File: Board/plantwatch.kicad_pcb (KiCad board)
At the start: 2 copper layers, 113 x 83.8 mm, 39 parts, among them IC1 HS1101, J1 Motor, J2 SEN0193, J3 SWD, J6 Power Input, Q1 BSP129, SW1 Reset, U1 MKL25Z128VLK4, U2 TMP36, U3 nRF24L01+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

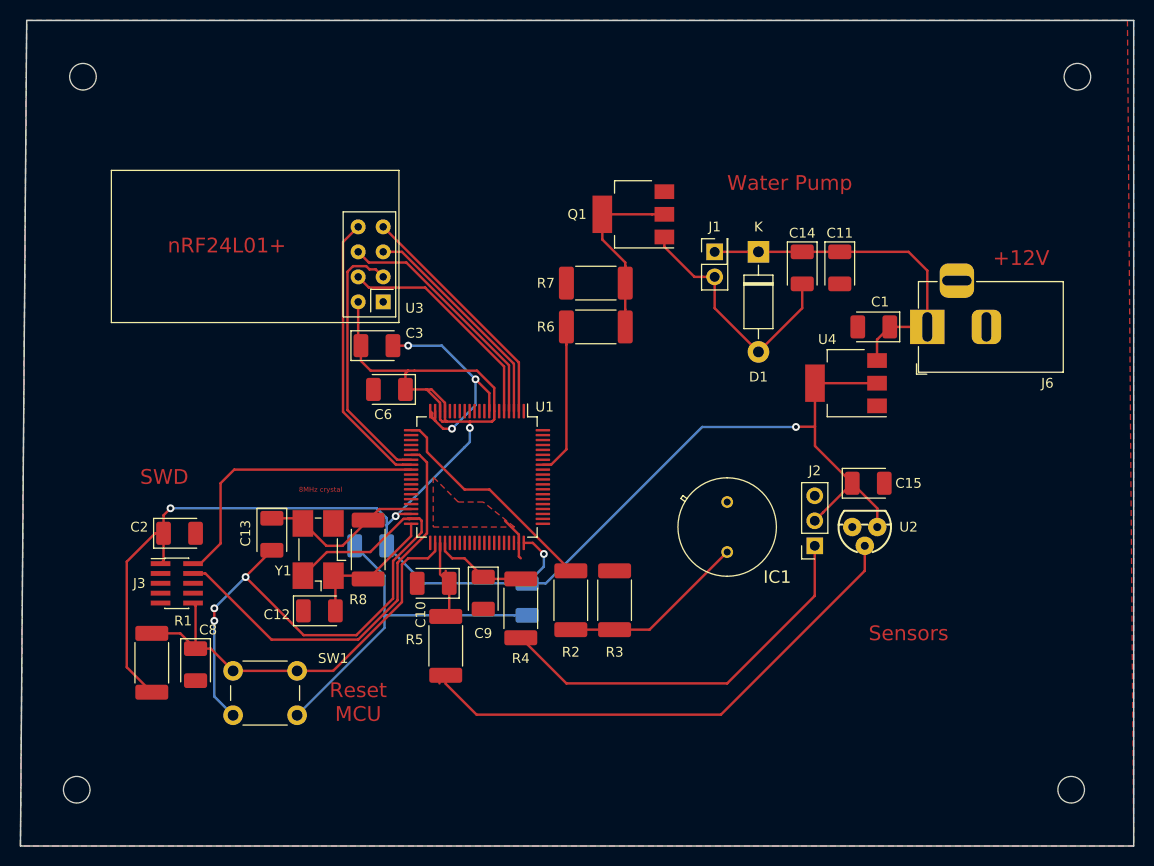
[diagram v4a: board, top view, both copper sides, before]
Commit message: SWD connector footprint pitch 1.0mm -> 1.27mm
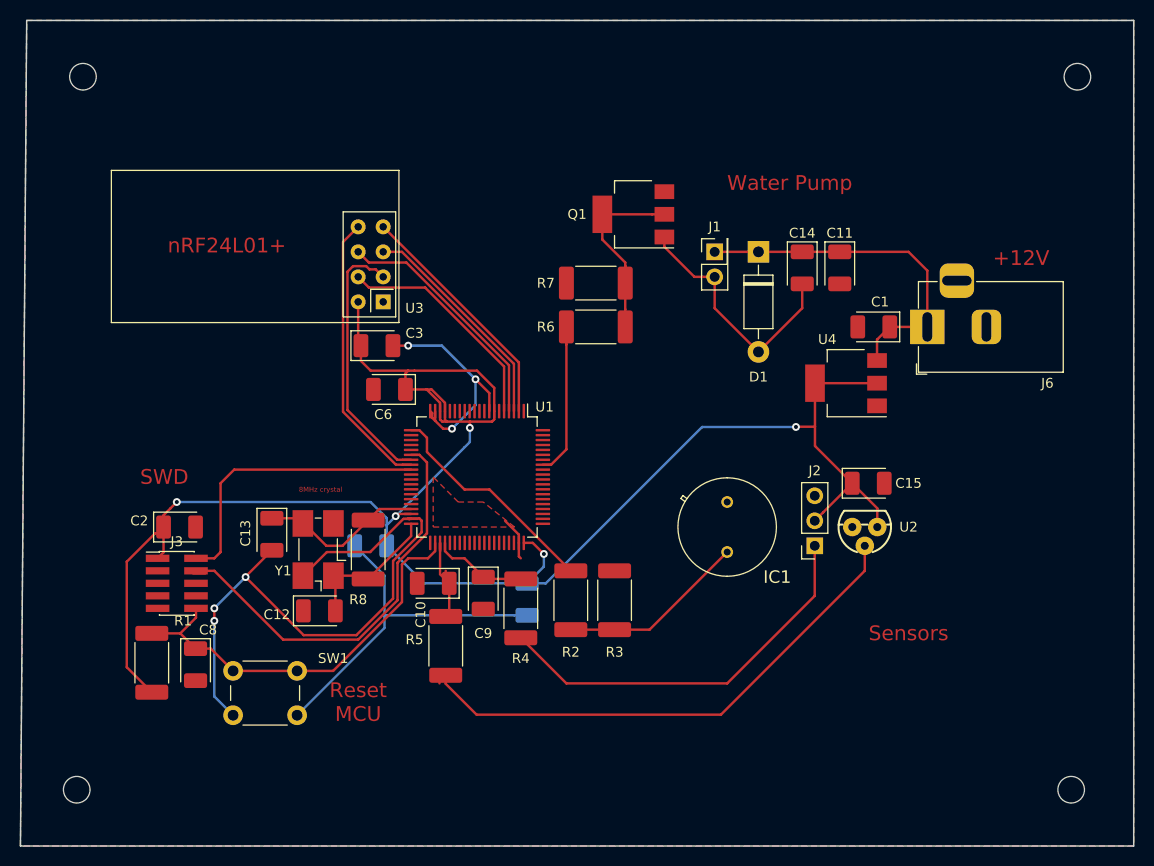
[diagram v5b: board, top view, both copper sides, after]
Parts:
- J3: footprint Connector_PinHeader_1.00mm:PinHeader_2x05_P1.00mm_Vertical_SMD -> Connector_PinHeader_1.27mm:PinHeader_2x05_P1.27mm_Vertical_SMD
- moved C2 0.64 mm to (71.2, 112.5)
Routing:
- net Net-(C8-Pad1): track 43.2 -> 41.7 mm
- net Net-(J3-Pad4): track 42.4 -> 43.4 mm
